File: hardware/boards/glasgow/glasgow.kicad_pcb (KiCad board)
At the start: 4 copper layers, 80 x 49 mm, 272 parts, among them J1 USB_C_USB2.0, J10 AUX, J2 IDC-Header_2x10_P2.54mm, J3 IDC-Header_2x10_P2.54mm, J4 Conn_01x02, J5 PinHeader_2x22_P1.27mm, J6 Conn_01x08, J7 Conn_01x08, J8 Conn_01x08, J9 Conn_01x08, SW1 RST, U1 CY7C68013A-56LTX, U10 SN74LVC1T45DCKR, U11 SN74LVC1T45DCKR, U12 INA233, U13 DAC081C081CIMK, U14 TPS73101DBV, U15 TPD3S014, U16 SN74LVC1T45DCKR, U17 SN74LVC1T45DCKR, U18 SN74LVC1T45DCKR, U19 PCA6408APW, U2 CAT24M01X, U20 DAC081C081CIMK, U21 INA233, U22 SN74LVC1T45DCKR, U23 SN74LVC1T45DCKR, U24 SN74LVC1T45DCKR, U25 SN74LVC1T45DCKR, U26 SN74LVC1T45DCKR, U27 SN74LVC1T45DCKR, U28 SN74LVC1T45DCKR, U29 SN74LVC1T45DCKR, U3 BL24C256A-SFRC, U30 ICE40HX8K-BG121, U31 TPS73101DBV, U32 SN74LVC1T45DCKR, U36 TLV73312PQDRVR, U4 SN74LVC1T45DCKR, U5 PCA6408APW, U6 SN74LVC1T45DCKR, U7 APX811-40UG-7, U8 TLV75533PDRVR, U9 SN74LVC1T45DCKR, Y1 24M

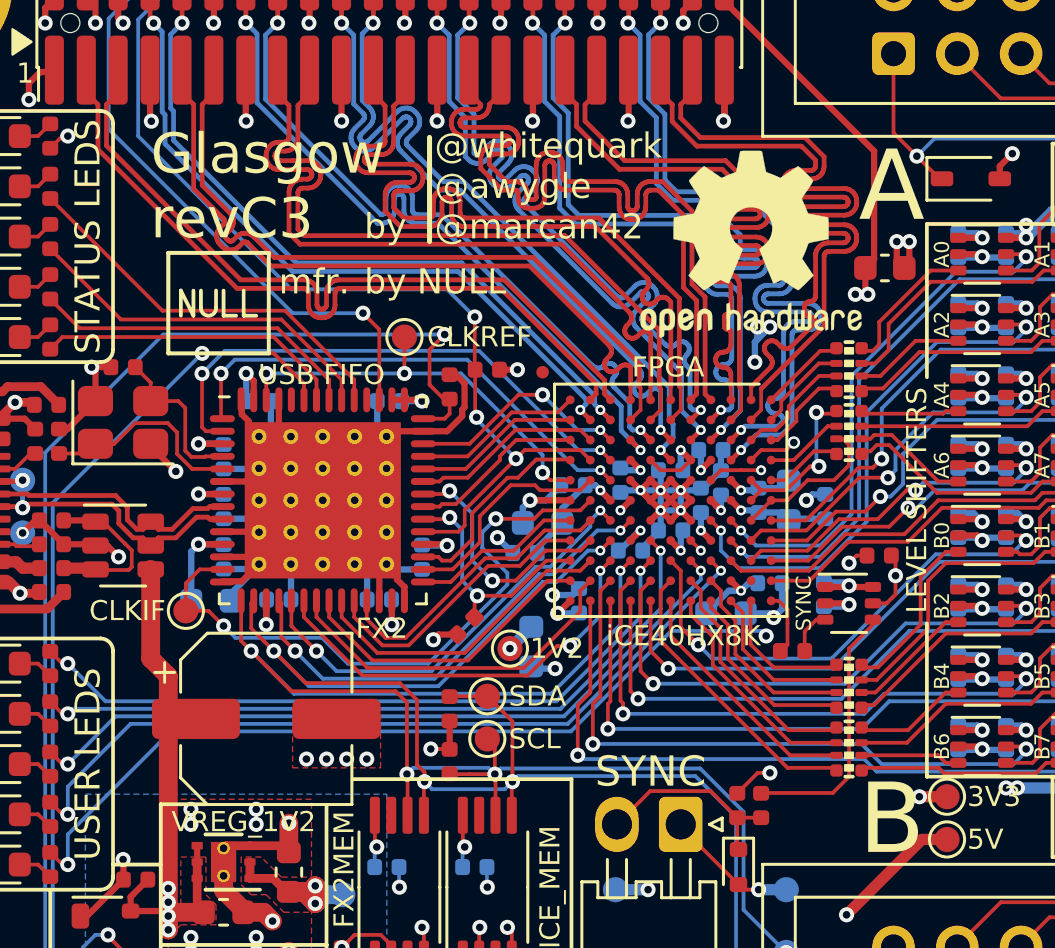
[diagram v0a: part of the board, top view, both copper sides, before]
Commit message: JLCPCB part swaps
Switch parts to be either of:
- cheaper
- in stock
- order-able
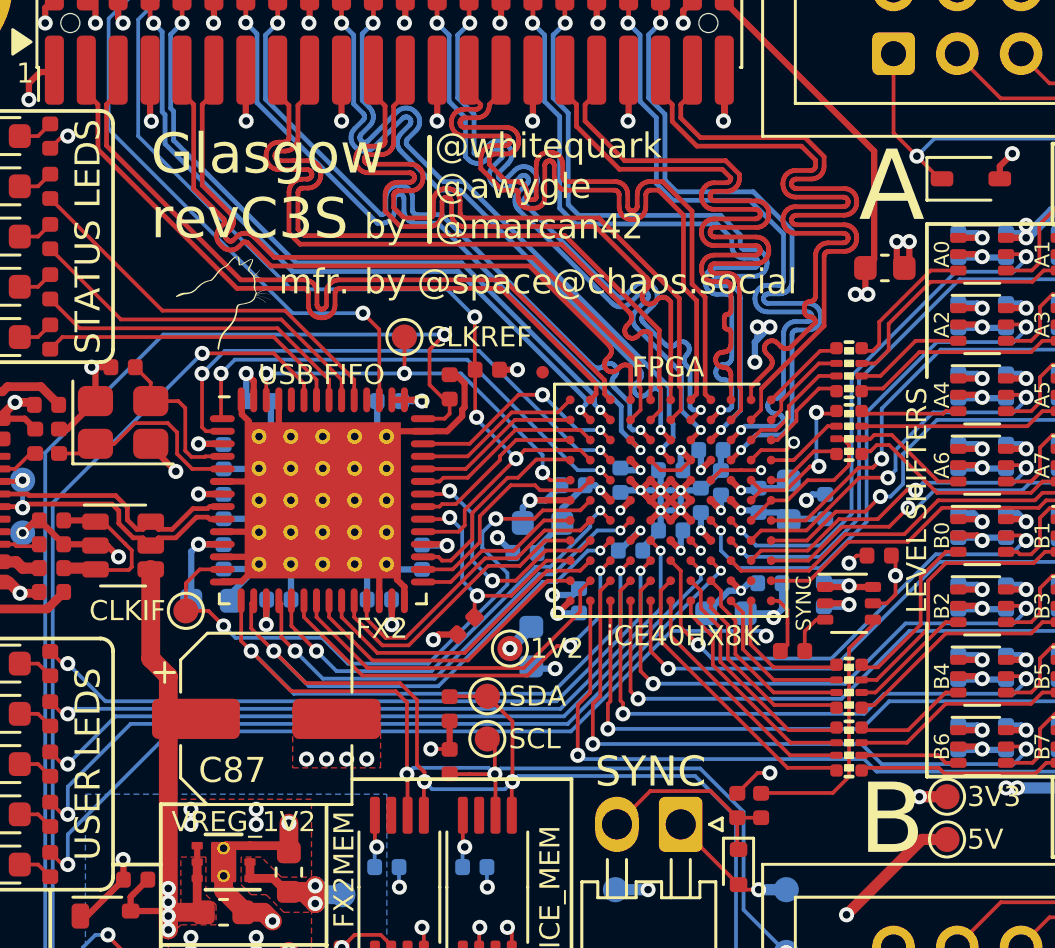
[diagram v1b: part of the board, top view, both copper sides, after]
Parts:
- removed the REF** at (86.9, 85.3)
- removed the REF** at (65.7, 87.7)
- removed the REF** at (59.5, 107.0)
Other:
- board text added: "@space@chaos.social"
- board text added: "Glasgow revC3S"
- board text added: "JLCJLCJLCJLC"
- board text added: "manufactured by @space"
- board text removed: "Glasgow revC3"
- board text removed: "NULL"
- board text removed: "manufactured by"
